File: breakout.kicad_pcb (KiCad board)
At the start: 2 copper layers, 103 x 62 mm, 32 parts, among them CON1 SD_Card, CON2 USB-MICRO-AB, P2 CONN_01X40, P3 CONN_01X40, P4 CONN_01X40, P5 A-DF-09-A/KG-T4S, SW1 SW_PUSH

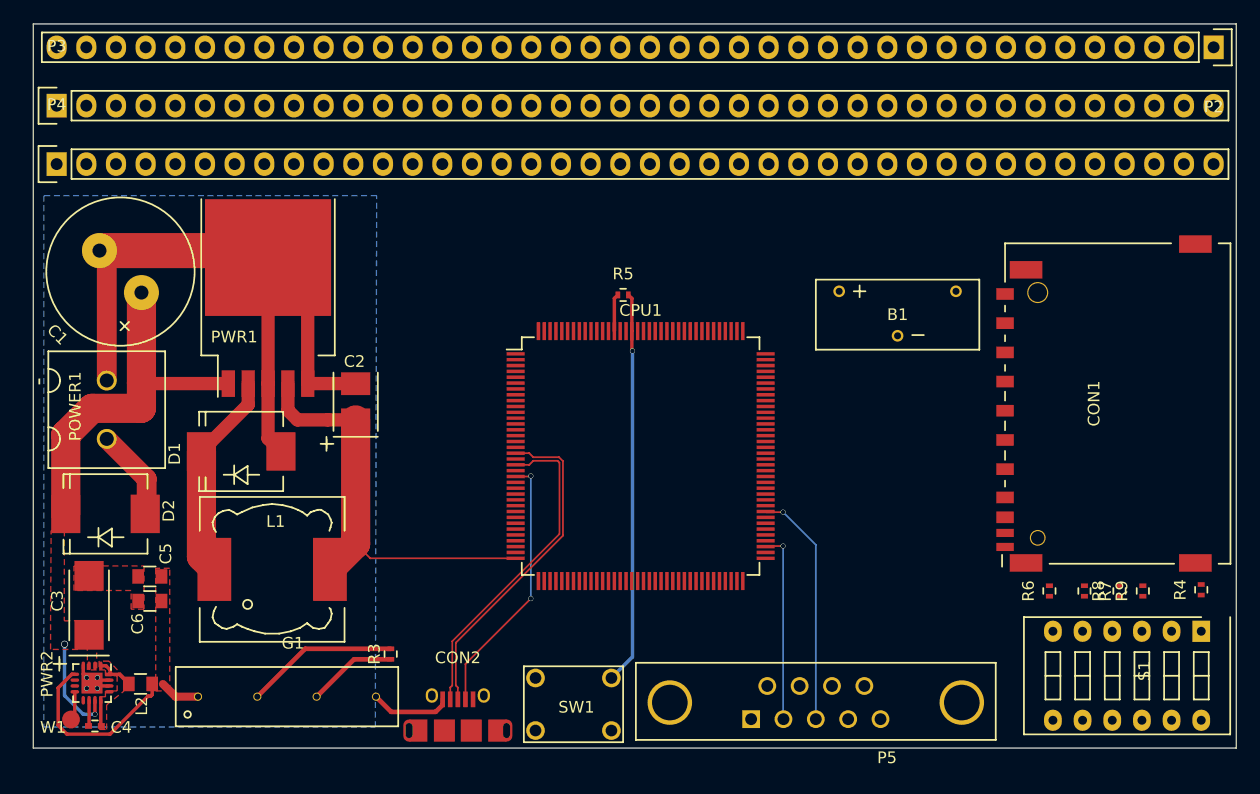
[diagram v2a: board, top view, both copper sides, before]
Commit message: routing IC left side traces
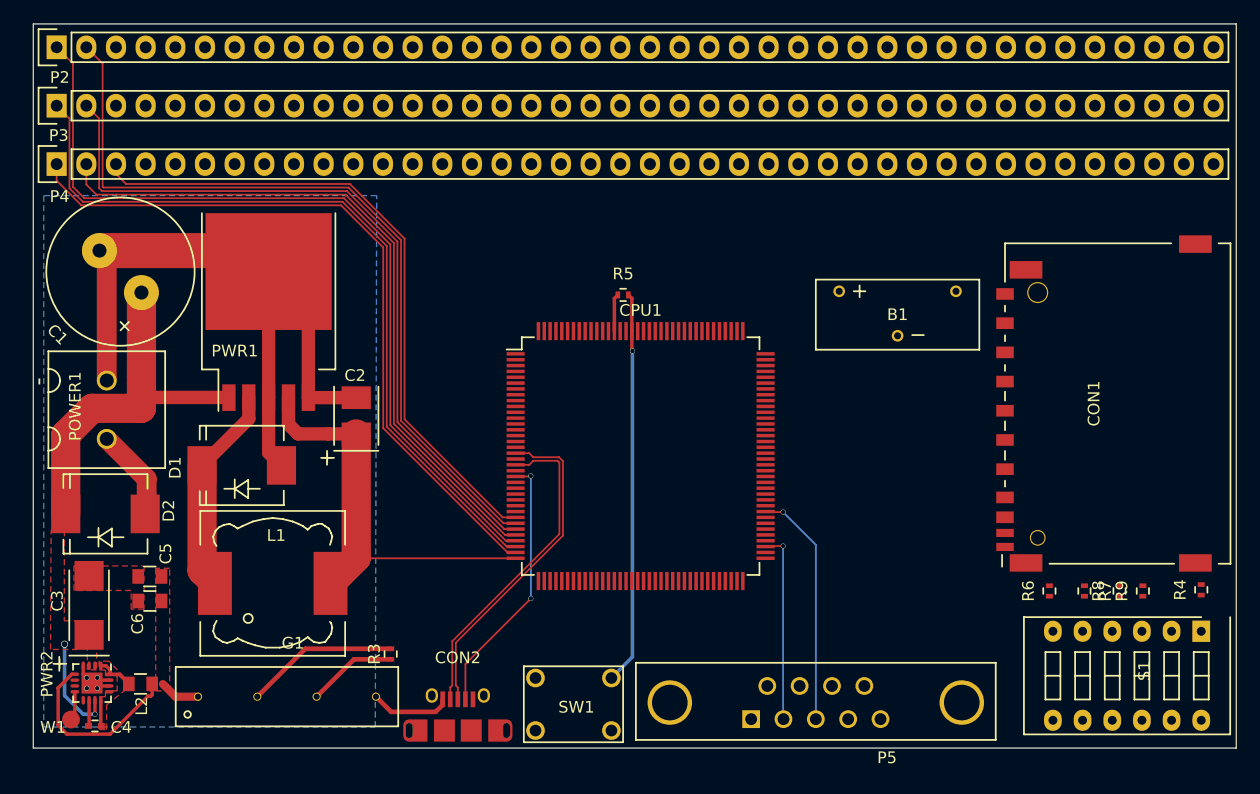
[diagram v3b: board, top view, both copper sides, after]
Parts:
- moved P2 99.1 mm to (60.0, 115.0), turned to 0 degrees
- moved PWR1 1.20 mm to (78.2, 145.0)
- moved D1 1.20 mm to (75.8, 150.8)
- moved L1 1.20 mm to (78.5, 160.9)
- moved C2 1.20 mm to (85.7, 146.5)
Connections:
- CPU1 pad 1: (no net) -> /P4_0
- CPU1 pad 10: (no net) -> /P4_5
- CPU1 pad 11: (no net) -> /P4_6
- CPU1 pad 12: (no net) -> /XTAL1
- CPU1 pad 13: (no net) -> /XTAL2
- CPU1 pad 14: (no net) -> /P4_7
- CPU1 pad 15: (no net) -> /P4_8
- CPU1 pad 2: (no net) -> /ADC0_1
- CPU1 pad 26: (no net) -> /TDI
- CPU1 pad 27: (no net) -> /TCK
- CPU1 pad 28: (no net) -> /DBGEN
- CPU1 pad 29: (no net) -> /TRST
- CPU1 pad 3: (no net) -> /P4_1
- CPU1 pad 30: (no net) -> /TMS
- CPU1 pad 31: (no net) -> /TDO
- CPU1 pad 33: (no net) -> /P4_9
- CPU1 pad 34: (no net) -> /P0_1
- CPU1 pad 35: (no net) -> /P4_10
- CPU1 pad 6: (no net) -> /ADC0_0
- CPU1 pad 7: (no net) -> /P4_3
- CPU1 pad 8: (no net) -> /P4_2
- CPU1 pad 9: (no net) -> /P4_4
- P2 pad 1: (no net) -> /P4_9
- P2 pad 2: (no net) -> /TMS
- P2 pad 3: (no net) -> /TCK
- P2 pad 4: (no net) -> /P4_7
- P2 pad 5: (no net) -> /P4_6
- P2 pad 6: (no net) -> /P4_2
- P2 pad 7: (no net) -> /P4_1
- P3 pad 1: (no net) -> /P0_1
- P3 pad 2: (no net) -> /TDO
- P3 pad 3: (no net) -> /DBGEN
- P3 pad 4: (no net) -> /P4_8
- P3 pad 5: (no net) -> /XTAL1
- P3 pad 6: (no net) -> /P4_4
- P3 pad 7: (no net) -> /ADC0_0
- P3 pad 8: (no net) -> /P4_0
- P4 pad 1: (no net) -> /P4_10
- P4 pad 2: (no net) -> /IC_WP
- P4 pad 3: (no net) -> /TRST
- P4 pad 4: (no net) -> /TDI
- P4 pad 5: (no net) -> /XTAL2
- P4 pad 6: (no net) -> /P4_5
- P4 pad 7: (no net) -> /P4_3
- P4 pad 8: (no net) -> /ADC0_1
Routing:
- net /P4_9: track 0.00 -> 72.0 mm
- net /TMS: track 0.00 -> 68.9 mm
- net /P0_1: track 0.00 -> 67.5 mm
- net /TDO: track 0.00 -> 64.3 mm
- net /P4_10: track 0.00 -> 63.0 mm
- net /IC_WP: track 0.00 -> 60.0 mm
- net /TRST: track 0.00 -> 56.3 mm
- net /3.3V: track 39.6 -> 37.8 mm
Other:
- net class Absolute Smallest: clearance 0.0762 -> 0.1524

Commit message: top side of IC routed
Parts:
- moved B1 27.6 mm to (105.3, 128.9)
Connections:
- CPU1 pad 110: (no net) -> /P7_0
- CPU1 pad 112: (no net) -> /P3_0
- CPU1 pad 113: (no net) -> /P7_1
- CPU1 pad 114: (no net) -> /P3_1
- CPU1 pad 115: (no net) -> /P7_2
- CPU1 pad 116: (no net) -> /P3_2
- CPU1 pad 117: (no net) -> /P7_3
- CPU1 pad 118: (no net) -> /SPI_SCK
- CPU1 pad 119: (no net) -> /P3_4
- CPU1 pad 120: (no net) -> /PF_4
- CPU1 pad 121: (no net) -> /P3_5
- CPU1 pad 122: (no net) -> /SPI_MISO
- CPU1 pad 123: (no net) -> /SPI_MOSI
- CPU1 pad 124: (no net) -> /SPI_SSEL
- CPU1 pad 125: (no net) -> /RTCX1
- CPU1 pad 126: (no net) -> /RTCX2
- CPU1 pad 129: (no net) -> /RTC_ALARM
- CPU1 pad 130: (no net) -> /WAKEUP0
- CPU1 pad 132: (no net) -> /P7_4
- CPU1 pad 133: (no net) -> /P7_5
- CPU1 pad 134: (no net) -> /P7_6
- CPU1 pad 136: (no net) -> /ADC0_7
- CPU1 pad 138: (no net) -> /ADC0_4
- CPU1 pad 139: (no net) -> /ADC0_3
- CPU1 pad 140: (no net) -> /P7_7
- CPU1 pad 142: (no net) -> /ADC0_6
- CPU1 pad 143: (no net) -> /ADC0_2
- CPU1 pad 144: (no net) -> /ADC0_5
- P2 pad 16: (no net) -> /ADC0_6
- P2 pad 17: (no net) -> /ADC0_4
- P2 pad 18: (no net) -> /P7_5
- P2 pad 19: (no net) -> /RTC_ALARM
- P2 pad 20: (no net) -> /SPI_SSEL
- P2 pad 21: (no net) -> /P3_5
- P2 pad 22: (no net) -> /SPI_SCK
- P2 pad 23: (no net) -> /P7_2
- P2 pad 24: (no net) -> /P3_0
- P3 pad 16: (no net) -> /ADC0_2
- P3 pad 17: (no net) -> /ADC0_3
- P3 pad 18: (no net) -> /P7_6
- P3 pad 19: (no net) -> /WAKEUP0
- P3 pad 20: (no net) -> /RTCX1
- P3 pad 21: (no net) -> /SPI_MISO
- P3 pad 22: (no net) -> /P3_4
- P3 pad 23: (no net) -> /P3_2
- P3 pad 24: (no net) -> /P7_1
- P4 pad 16: (no net) -> /ADC0_5
- P4 pad 17: (no net) -> /P7_7
- P4 pad 18: (no net) -> /ADC0_7
- P4 pad 19: (no net) -> /P7_4
- P4 pad 20: (no net) -> /RTCX2
- P4 pad 21: (no net) -> /SPI_MOSI
- P4 pad 22: (no net) -> /PF_4
- P4 pad 23: (no net) -> /P7_3
- P4 pad 24: (no net) -> /P3_1
- P4 pad 25: (no net) -> /P7_0
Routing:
- net /IC_WP: track 60.0 -> 129.8 mm, vias 0 -> 1
- net /P1_1: track 0.00 -> 53.3 mm
- net /P1_2: track 0.00 -> 49.4 mm
- net /ISP_ENABLE: track 0.00 -> 45.8 mm, vias 0 -> 1
- net /P2_8: track 0.00 -> 35.9 mm, vias 0 -> 1
- net /P2_9: track 0.00 -> 33.2 mm, vias 0 -> 1
- net /ADC0_6: track 0.00 -> 26.0 mm
- net /P3_0: track 0.00 -> 25.9 mm
- net /SPI_SSEL: track 0.00 -> 25.9 mm
- net /ADC0_4: track 0.00 -> 25.8 mm
- net /P7_5: track 0.00 -> 25.8 mm
- net /RTC_ALARM: track 0.00 -> 25.6 mm, vias 0 -> 1
- net /P7_2: track 0.00 -> 25.6 mm
- net /P3_5: track 0.00 -> 25.1 mm
- net /SPI_SCK: track 0.00 -> 25.1 mm
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
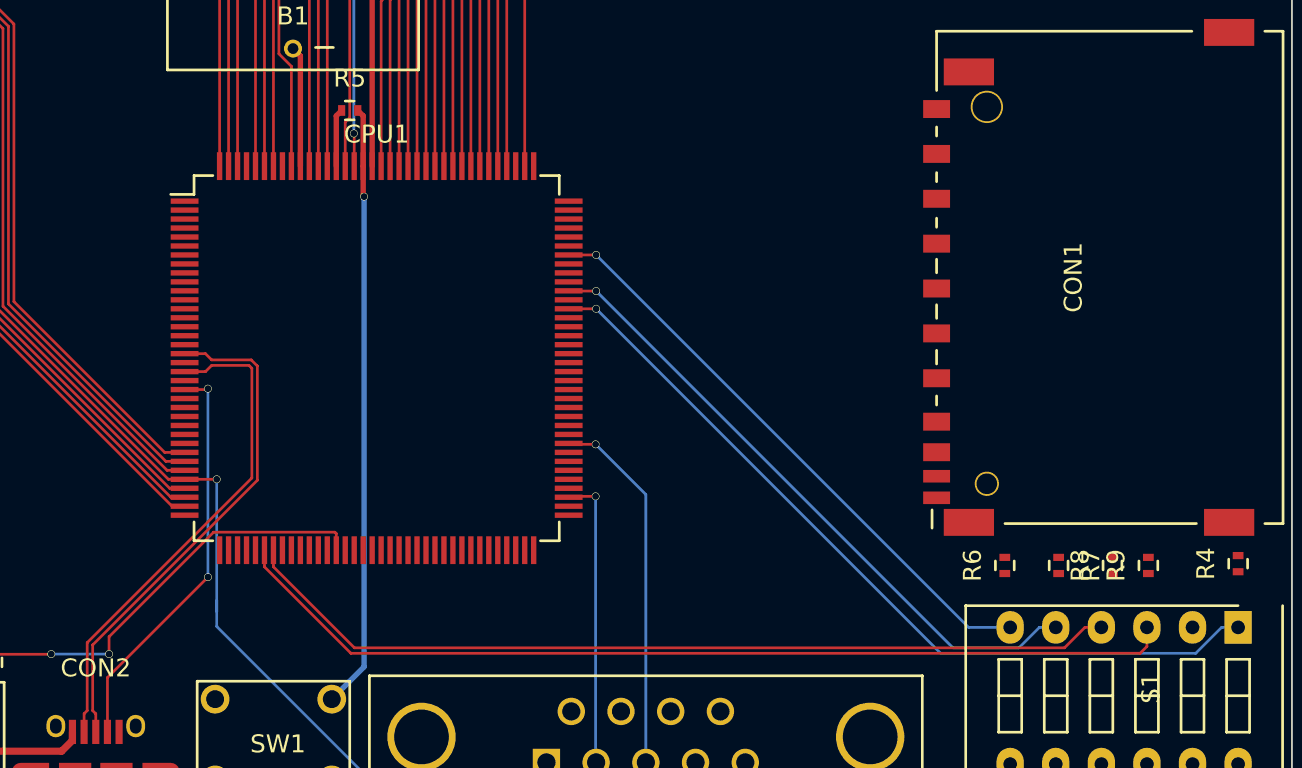
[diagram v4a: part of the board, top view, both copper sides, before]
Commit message: routed SD card socket and DIP switches
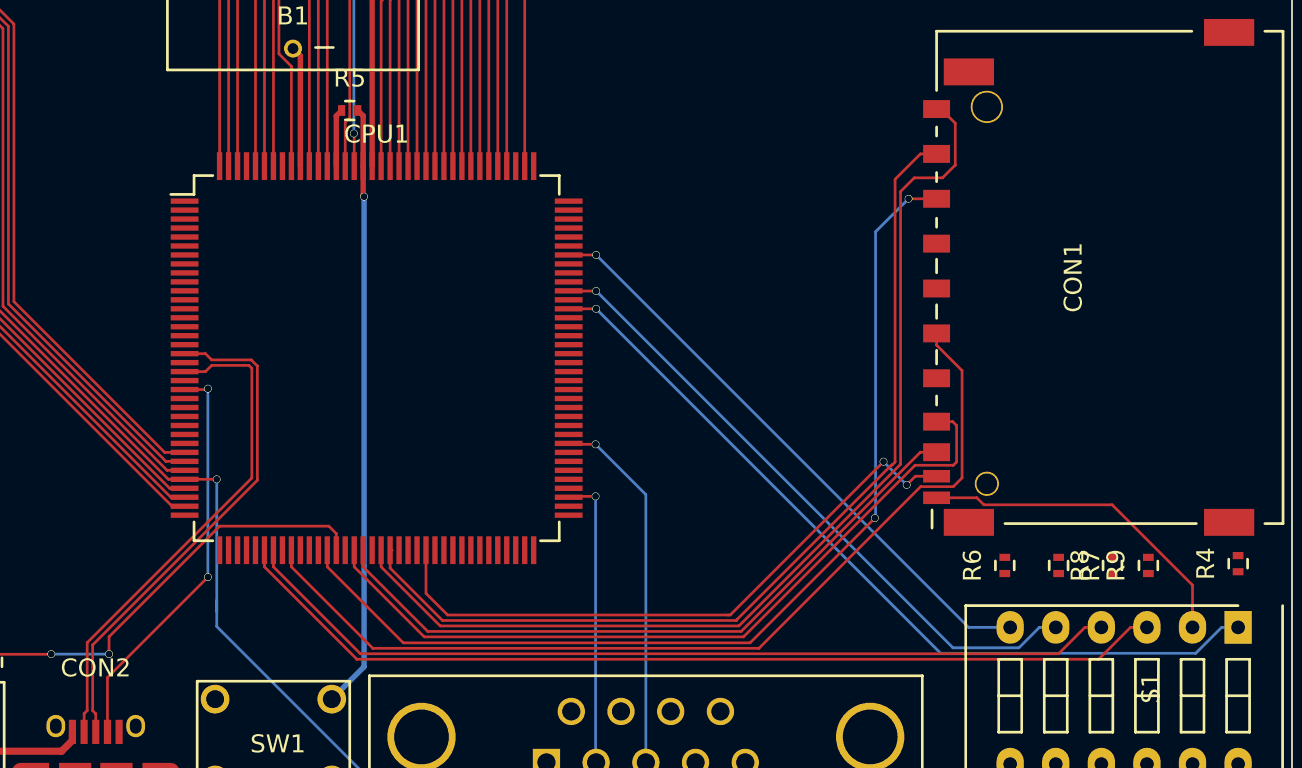
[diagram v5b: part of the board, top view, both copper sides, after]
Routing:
- net /SD_DAT2: track 0.00 -> 57.5 mm
- net /SD_CMD: track 0.00 -> 56.2 mm, vias 0 -> 2
- net /SD_DAT3: track 0.00 -> 52.8 mm
- net /SD_CLK: track 0.00 -> 52.8 mm
- net /SD_DAT0: track 0.25 -> 43.9 mm
- net /SD_DAT1: track 0.25 -> 38.5 mm
- net /SD_CD: track 0.00 -> 35.6 mm, vias 0 -> 2
- net /SD_WP: track 0.00 -> 18.6 mm

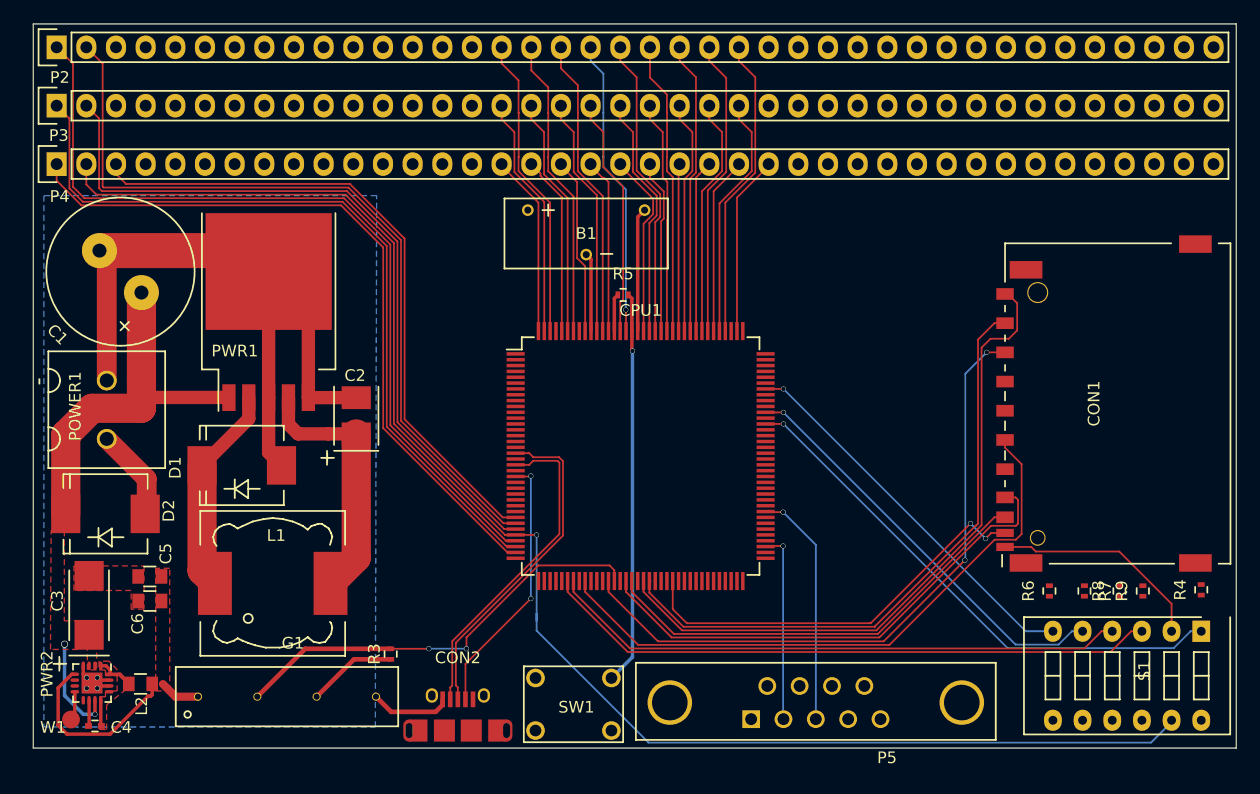
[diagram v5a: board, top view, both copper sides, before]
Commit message: routed lower-left of IC
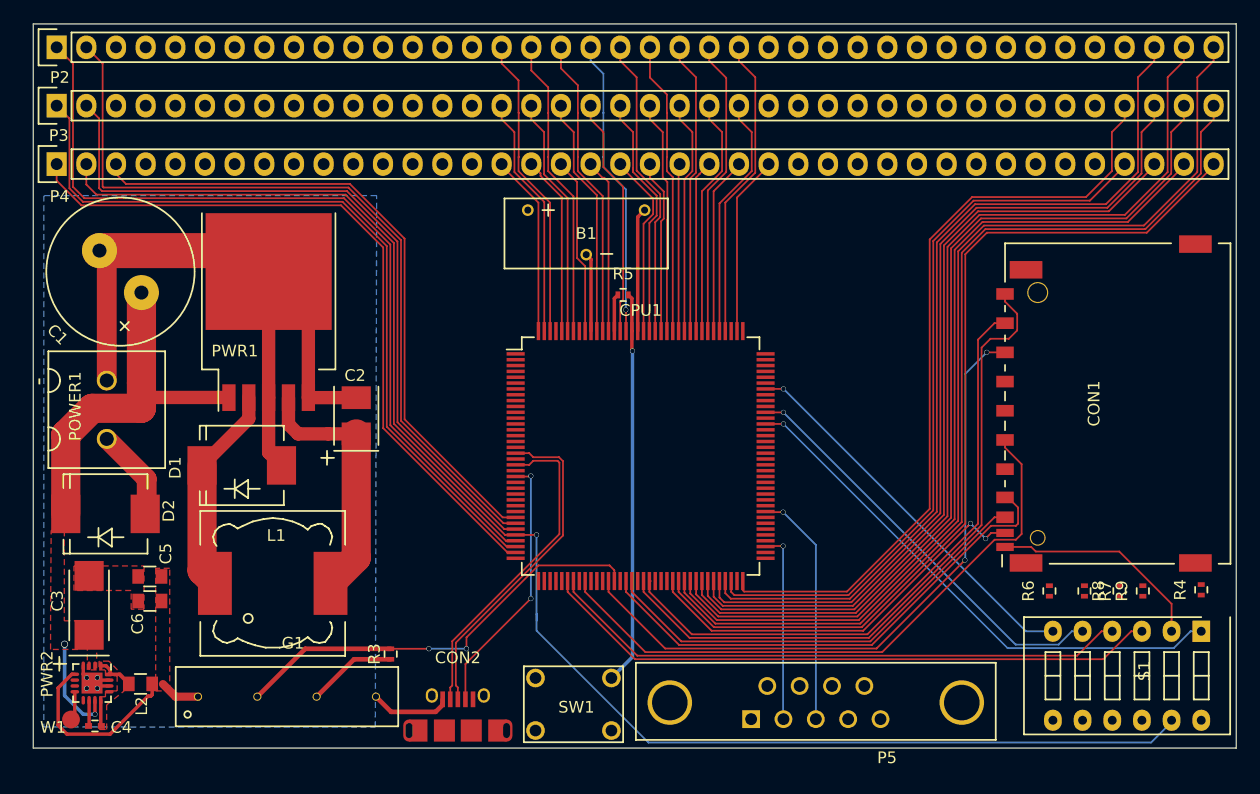
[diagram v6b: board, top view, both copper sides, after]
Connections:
- CPU1 pad 61: (no net) -> /P1_14
- CPU1 pad 62: (no net) -> /P1_15
- CPU1 pad 63: (no net) -> /P5_6
- CPU1 pad 64: (no net) -> /P1_16
- CPU1 pad 65: (no net) -> /P5_7
- CPU1 pad 66: (no net) -> /P1_17
- CPU1 pad 67: (no net) -> /P1_18
- CPU1 pad 68: (no net) -> /P1_19
- CPU1 pad 69: (no net) -> /P9_5
- CPU1 pad 70: (no net) -> /P1_20
- CPU1 pad 72: (no net) -> /P9_6
- P2 pad 38: (no net) -> /P9_5
- P2 pad 39: (no net) -> /P1_17
- P2 pad 40: (no net) -> /P5_6
- P3 pad 37: (no net) -> /P9_6
- P3 pad 38: (no net) -> /P1_19
- P3 pad 39: (no net) -> /P5_7
- P3 pad 40: (no net) -> /P1_15
- P4 pad 37: (no net) -> /P1_20
- P4 pad 38: (no net) -> /P1_18
- P4 pad 39: (no net) -> /P1_16
- P4 pad 40: (no net) -> /P1_14
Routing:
- net /P5_6: track 0.00 -> 86.1 mm
- net /P1_15: track 0.00 -> 82.0 mm
- net /P1_17: track 0.00 -> 81.4 mm
- net /P1_14: track 0.00 -> 78.0 mm
- net /P5_7: track 0.00 -> 77.4 mm
- net /P9_5: track 0.00 -> 76.5 mm
- net /P1_16: track 0.00 -> 73.3 mm
- net /P1_19: track 0.00 -> 72.7 mm
- net /P1_18: track 0.00 -> 68.7 mm
- net /P9_6: track 0.00 -> 66.9 mm
- net /P1_20: track 0.00 -> 63.6 mm
- net /SD_DAT1: track 38.5 -> 39.0 mm
- net /SD_CMD: track 56.2 -> 56.7 mm
- net /SD_CLK: track 52.8 -> 53.3 mm
- net /P1_2: track 49.7 -> 50.2 mm
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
